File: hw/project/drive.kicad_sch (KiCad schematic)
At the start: 63 parts, among them Q10 STL110N10F7, Q5 STL110N10F7, Q6 STL110N10F7, Q7 STL110N10F7, Q8 STL110N10F7, Q9 STL110N10F7

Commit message: Continuing power revamp tomorrow
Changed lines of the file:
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@@
 		(exclude_from_sim no)
 		(at 220.98 38.1001 0)
-		(size 93.98 22.8453)
+		(size 93.98 20.3199)
 		(margins 0.9525 0.9525 0.9525 0.9525)
 		(stroke
@@
 		)
 	)
-	(text_box "Shunt Resistor\n\nFor a +/-50mV drop at +/-50A, R = 1.0m = 2.0m || 2.0m\n\nPair of parallel resistors, so 50A cts => 2.5W total (> 1.25W each)\n\nAt +/-2A, drop is +/-2mV, but use OPAMP configured in PGA mode (and voltage bias from internal DAC connection) to map to ADC range accordingly (bench testing will use way higher gain than while riding it fr)\n\nReason for not having an external resistor network for current sensing is it would mean a fixed gain, thus it could not be flexible for both bench testing and actually riding\n\nLayout Note: Using just regular 2-pin resistors despite the choice of symbol (4-pin kelvin sense)\n\nFW Note: Implement OCP (5.5.2 in UM2896) all in firmware by routing OPO_x to COMPx's non-inverting input and compared against the corresponding overcurrent threshoold voltage generated by an internal DAC. If an OCP event occurs, the comparator trips the TIM1_BKIN line, which shuts down the gate driver outputs"
+	(text_box "Shunt Resistor\n\nFor a +/-50mV drop at +/-50A, R = 1.0m = 2.0m || 2.0m\n\nPair of parallel resistors, so 50A cts => 2.5W total (> 1.25W each)\n\nAt +/-2A, drop is +/-2mV, but use OPAMP configured in PGA mode (and voltage bias from internal DAC connection) to map to ADC range accordingly (bench testing will use way higher gain than while riding it fr)\n\nReason for not having an external resistor network for current sensing is it would mean a fixed gain, thus it could not be flexible for both bench testing and actually riding\n\nLayout Note: Using just regular 2-pin resistors despite the choice of symbol (4-pin kelvin sense)\n\nFW Notes: \n- Implement OCP (5.5.2 in UM2896) all in firmware by routing OPO_x to COMPx's non-inverting input and compared against the corresponding overcurrent threshoold voltage generated by an internal DAC. If an OCP event occurs, the comparator trips the TIM1_BKIN line, which shuts down the gate driver outputs"
 		(exclude_from_sim no)
-		(at 220.98 60.9601 0)
-		(size 93.98 45.7199)
+		(at 220.98 58.4199 0)
+		(size 93.98 48.2601)
 		(margins 0.9525 0.9525 0.9525 0.9525)
 		(stroke

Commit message: Checkpoint: Ready to spec rest of power stage tom
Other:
- note added: "reconcile 22 vs 22.1k??"
- note added: "verify all with claude!!!!!!!!!!!!!!!!!!!!!!"
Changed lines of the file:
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@@
+		)
+	)
+	(text "verify all with claude!!!!!!!!!!!!!!!!!!!!!!"
+		(exclude_from_sim no)
+		(at -10.16 154.686 0)
+		(effects
+			(font
+				(size 1.27 1.27)
+				(color 255 4 4 1)
+			)
+			(justify left)
 		)
 	)
@@
 			)
 			(justify left top)
+		)
+	)
+	(text "reconcile 22 vs 22.1k??"
+		(exclude_from_sim no)
+		(at 13.97 171.196 0)
+		(effects
+			(font
+				(size 1.27 1.27)
+				(color 255 4 4 1)
+			)
+			(justify left)
 		)
 	)
@@
 		)
 	)
-	(text_box "Shunt Resistor\n\nFor a +/-50mV drop at +/-50A, R = 1.0m = 2.0m || 2.0m\n\nPair of parallel resistors, so 50A cts => 2.5W total (> 1.25W each)\n\nAt +/-2A, drop is +/-2mV, but use OPAMP configured in PGA mode (and voltage bias from internal DAC connection) to map to ADC range accordingly (bench testing will use way higher gain than while riding it fr)\n\nReason for not having an external resistor network for current sensing is it would mean a fixed gain, thus it could not be flexible for both bench testing and actually riding\n\nLayout Note: Using just regular 2-pin resistors despite the choice of symbol (4-pin kelvin sense)\n\nFW Notes: \n- Implement OCP (5.5.2 in UM2896) all in firmware by routing OPO_x to COMPx's non-inverting input and compared against the corresponding overcurrent threshoold voltage generated by an internal DAC. If an OCP event occurs, the comparator trips the TIM1_BKIN line, which shuts down the gate driver outputs"
+	(text_box "Shunt Resistor\n\nFor a +/-50mV drop at +/-50A, R = 1.0m = 2.0m || 2.0m\n\nPair of parallel resistors, so 50A cts => 2.5W total (> 1.25W each)\n\nAt +/-2A, drop is +/-2mV, but use OPAMP configured in PGA mode (and voltage bias from internal DAC connection) to map to ADC range accordingly (bench testing will use way higher gain than while riding it fr)\n\nReason for not having an external resistor network for current sensing is it would mean a fixed gain, thus it could not be flexible for both bench testing and actually riding\n\nLayout Note: \n- Using just regular 2-pin resistors despite the choice of symbol (4-pin kelvin sense)\n- Use Kelvin (differential trace pair) connections from inner pads to input pins\n\nFW Notes: \n- Implement OCP (5.5.2 in UM2896) all in firmware by routing OPO_x to COMPx's non-inverting input and compared against the corresponding overcurrent threshoold voltage generated by an internal DAC. If an OCP event occurs, the comparator trips the TIM1_BKIN line, which shuts down the gate driver outputs"
 		(exclude_from_sim no)
 		(at 220.98 58.4199 0)

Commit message: Spec bulk caps
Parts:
- added C20, C31: 22uF/100V, symbol Device:C_Small
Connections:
- net PGND: now also C20.2
- net VM: now also C20.1
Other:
- note added: "1210 or 2220"
- note added: "Bulk (Ceramic) Capacitor Bank"

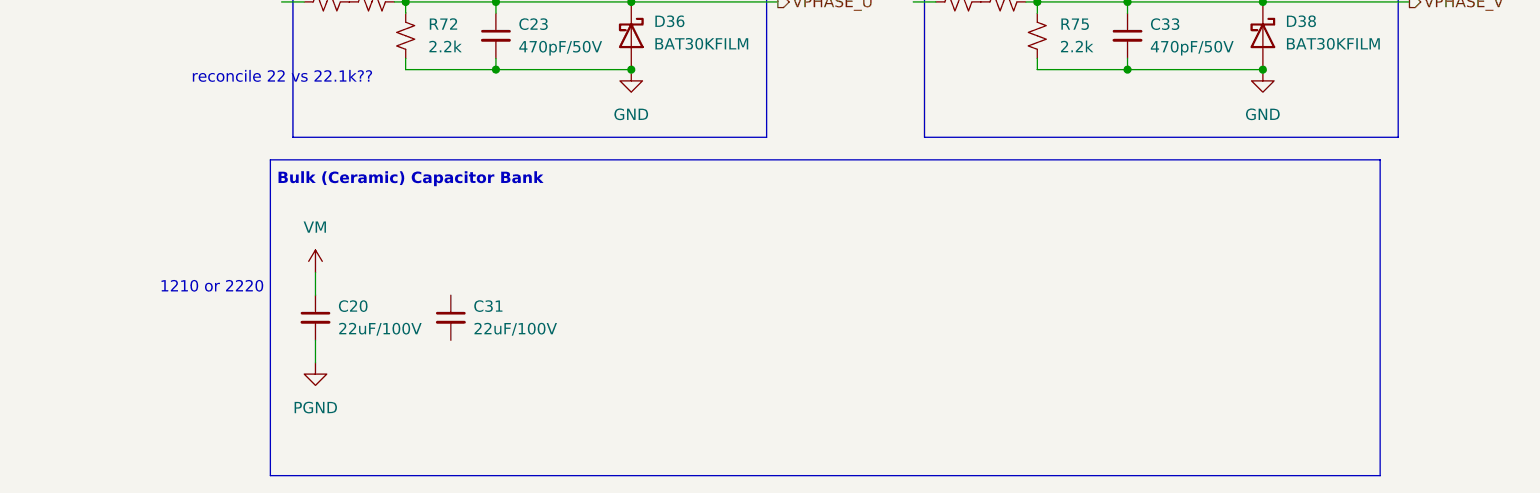
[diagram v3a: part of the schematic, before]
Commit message: Finalize 5V buck regulator
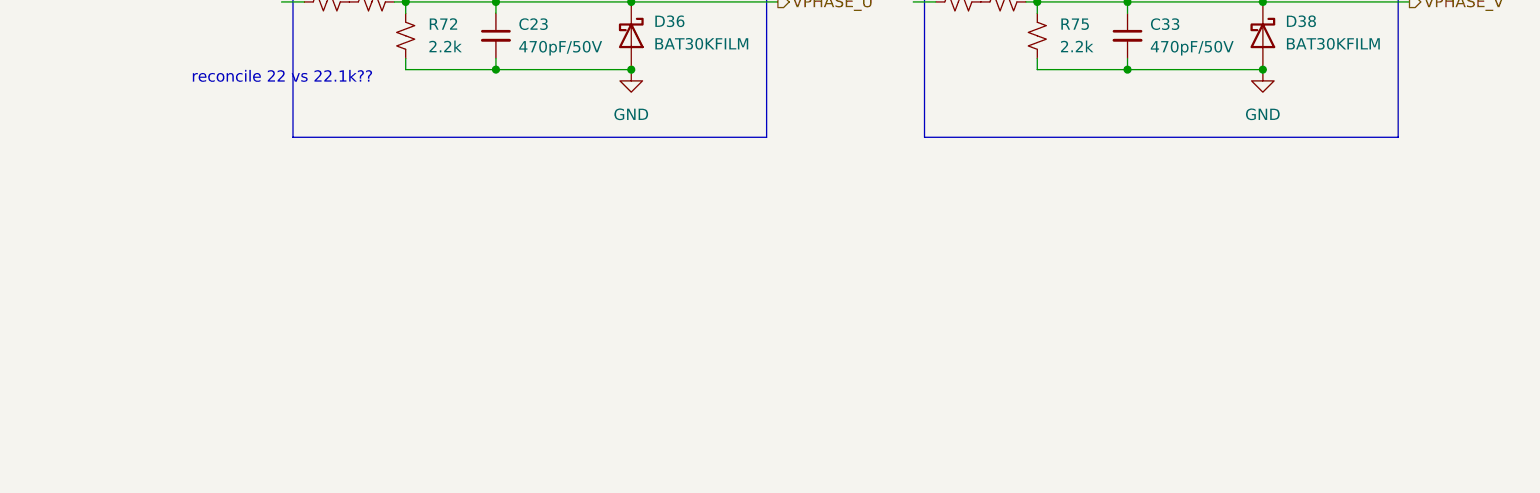
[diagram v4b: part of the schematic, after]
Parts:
- removed C20, C31: 22uF/100V, symbol Device:C_Small
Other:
- note removed: "1210 or 2220"
- note removed: "Bulk (Ceramic) Capacitor Bank"

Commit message: Spec LEDs
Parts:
- removed R52, R7, R70, R74, R76, R77: 22k, Resistor_SMD:R_0603_1608Metric, symbol Device:R_Small_US
- added R19, R24, R25, R26, R27, R30: 22.1k, Resistor_SMD:R_0603_1608Metric, symbol Device:R_Small_US
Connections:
- net U: now also R19.1
- net V: now also R25.1
- net VPHASE_U: now also R24.2
- net VPHASE_V: now also R26.2
- net VPHASE_W: now also R30.2
- net W: now also R27.1
- new net: R27.2, R30.1
- new net: R19.2, R24.1
- new net: R25.2, R26.1
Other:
- note added: "R2/(R1+R2) = 0.04741 {60} [V] -> {2.845} [V]"
- note removed: "R2/(R1+R2) = 1/21 = 0.04762 {60} [V] -> {2.857} [V]"
- note removed: "reconcile 22 vs 22.1k??"

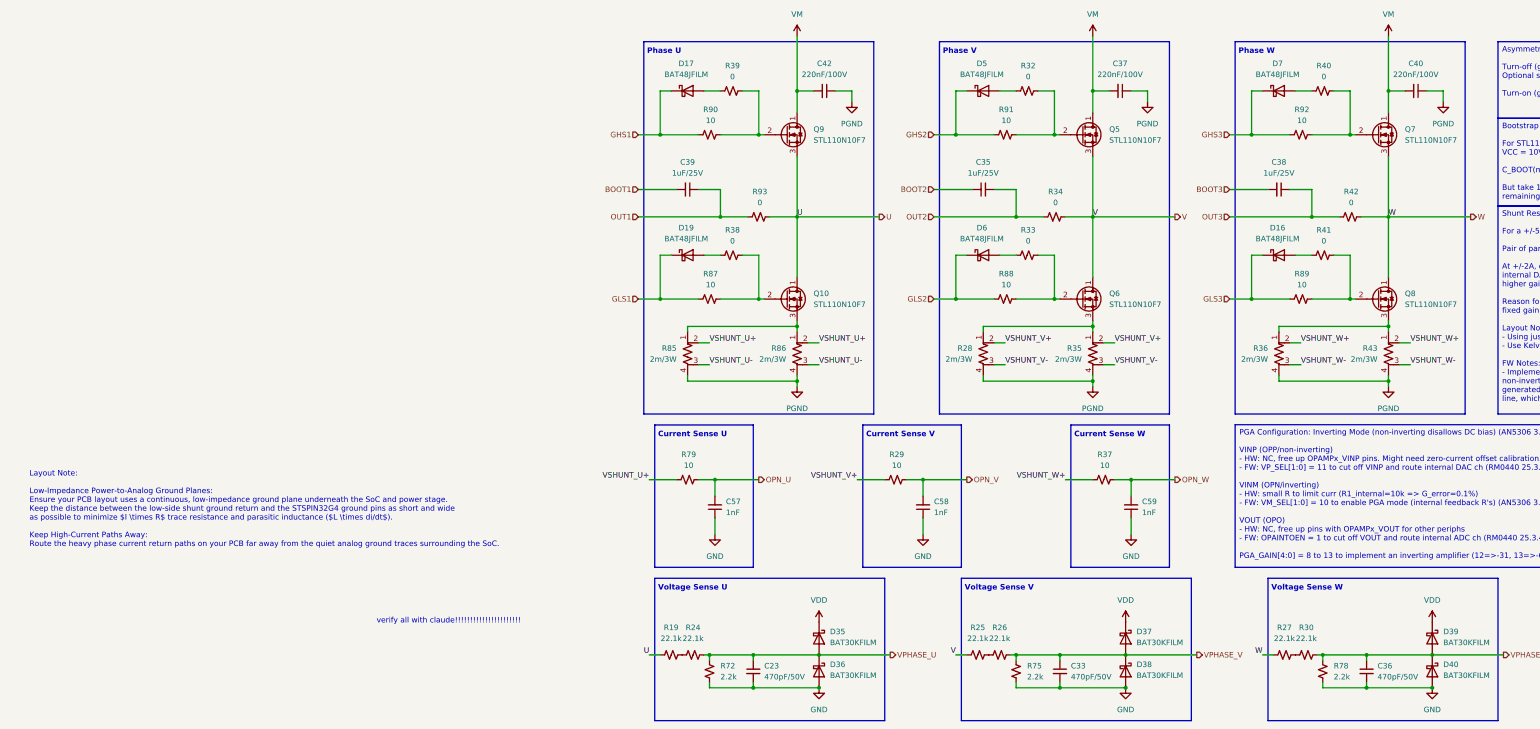
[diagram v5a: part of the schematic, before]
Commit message: Fixed annotations and H-labels
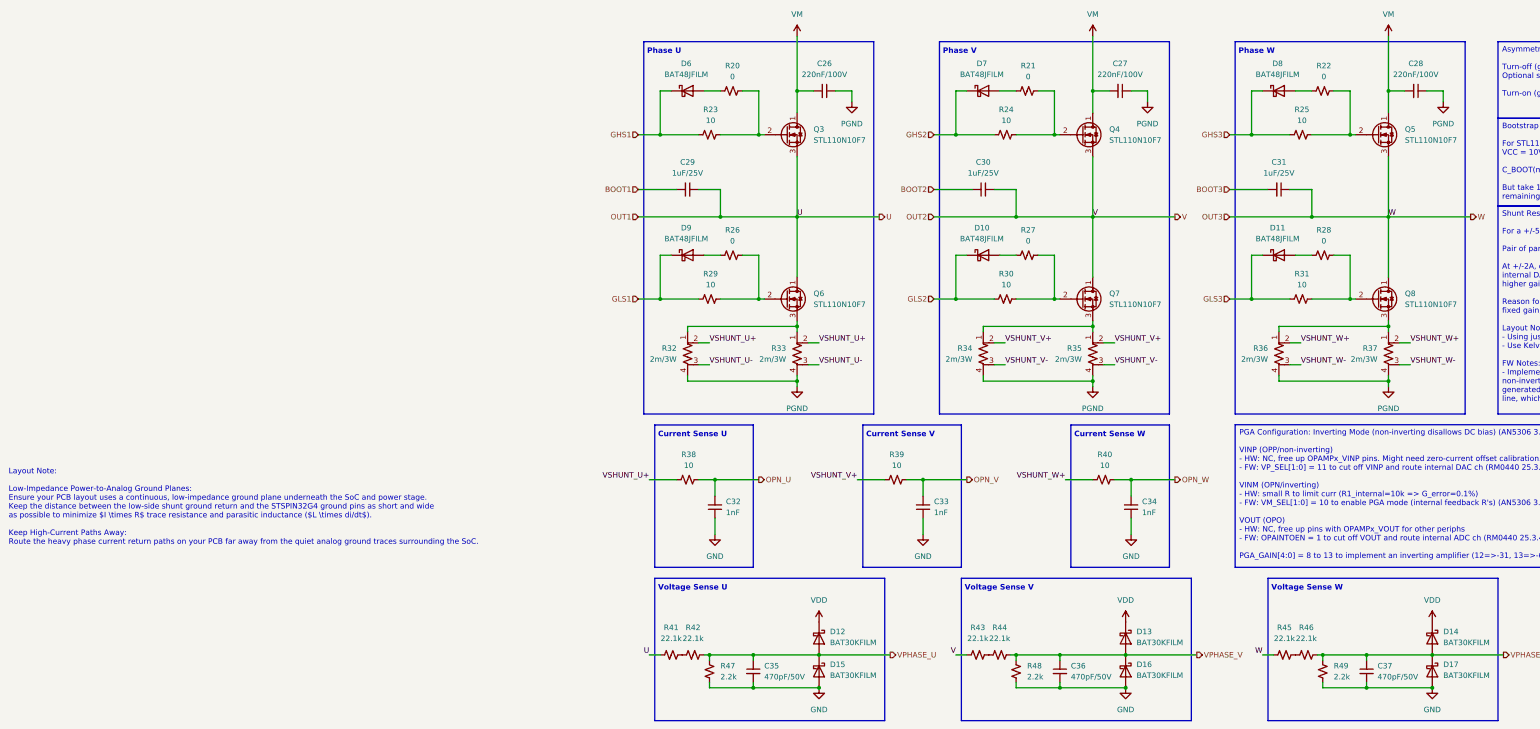
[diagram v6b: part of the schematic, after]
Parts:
- removed R34, R42, R93: 0, Resistor_SMD:R_0603_1608Metric, symbol Device:R_Small_US
- renumbered C42 to C26, C37 to C27, C40 to C28, C39 to C29, C35 to C30, C38 to C31, C57 to C32, C58 to C33, C59 to C34, C23 to C35, C33 to C36, C36 to C37, D6 to D10, D16 to D11, D35 to D12, D37 to D13, D39 to D14, D36 to D15, D38 to D16, D40 to D17, D17 to D6, D5 to D7, D7 to D8, D19 to D9, Q9 to Q3, Q5 to Q4, Q7 to Q5, Q10 to Q6, Q6 to Q7, R39 to R20, R32 to R21, R40 to R22, R90 to R23, R91 to R24, R92 to R25, R38 to R26, R33 to R27, R41 to R28, R87 to R29, R88 to R30, R89 to R31, R85 to R32, R86 to R33, R28 to R34, R43 to R37, R79 to R38, R29 to R39, R37 to R40, R19 to R41, R24 to R42, R25 to R43, R26 to R44, R27 to R45, R30 to R46, R72 to R47, R75 to R48, R78 to R49
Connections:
- net U is gone; now on net OUT1: Q3.3 (S), Q6.1 (D), R41.1
- net V is gone; now on net OUT2: Q4.3 (S), Q7.1 (D), R43.1
- net W is gone; now on net OUT3: Q5.3 (S), Q8.1 (D), R45.1
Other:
- note removed: "verify all with claude!!!!!!!!!!!!!!!!!!!!!!"

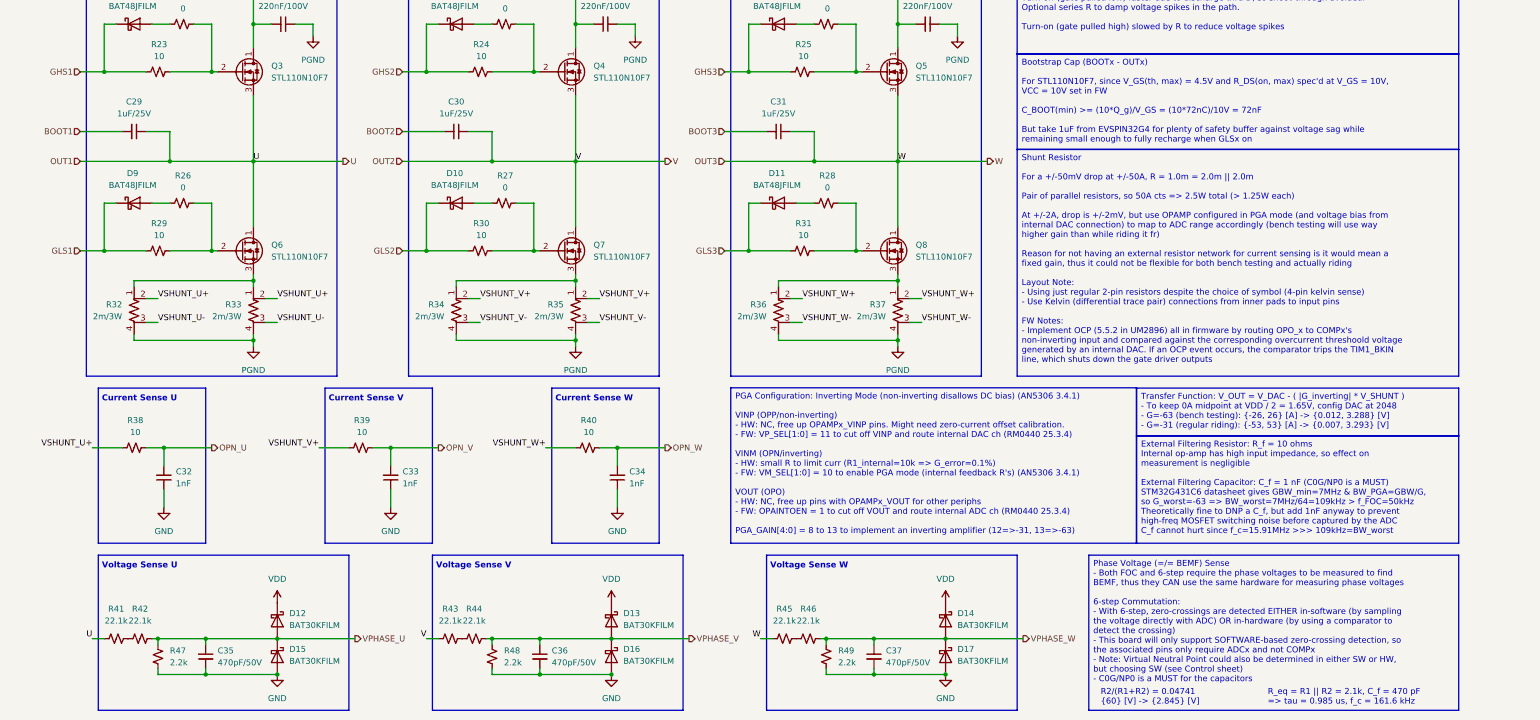
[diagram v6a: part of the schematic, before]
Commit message: Update shunt resistors and resolve ERC errors
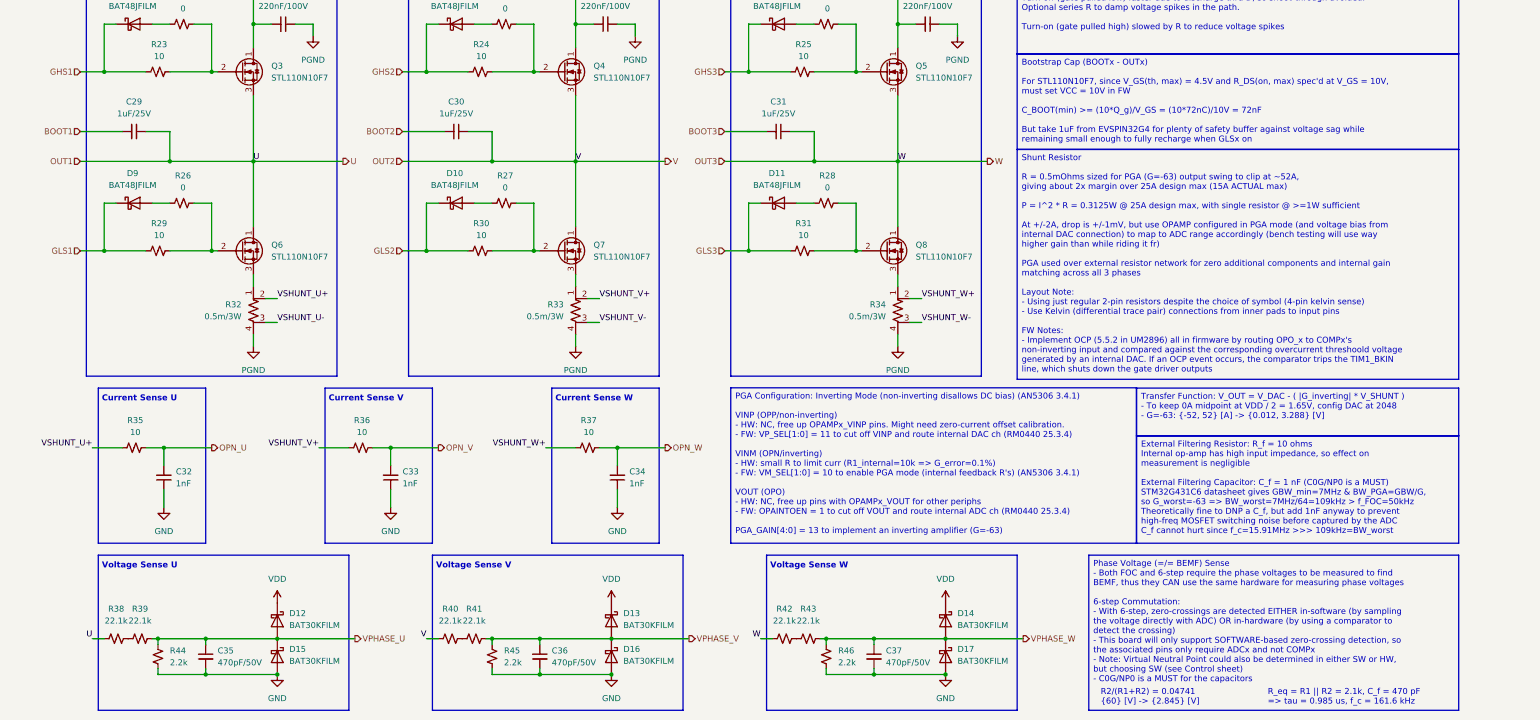
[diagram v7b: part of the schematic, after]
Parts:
- removed R32, R35, R36, R37: 2m/3W, Resistor_SMD:R_2512_6332Metric, symbol Device:R_Shunt_US
- added R33: 0.5m/3W, Resistor_SMD:R_2512_6332Metric, symbol Device:R_Shunt_US
- R32: renamed from R33; value 2m/3W -> 0.5m/3W
- R34: value 2m/3W -> 0.5m/3W
- renumbered R38 to R35, R39 to R36, R40 to R37, R41 to R38, R42 to R39, R43 to R40, R44 to R41, R45 to R42, R46 to R43, R47 to R44, R48 to R45, R49 to R46
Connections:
- net PGND: now also R33.4
- net VSHUNT_V+: now also R33.2; no longer R34.2
- net VSHUNT_V-: now also R33.3; no longer R34.3
- net VSHUNT_W+: now also R34.2
- net VSHUNT_W-: now also R34.3
- net at Q8.3 (S): now also R34.1
- net at Q7.3 (S): now also R33.1; no longer R34.1

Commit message: Clear PCB-add errors
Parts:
- R32, R33, R34: symbol Device:R_Shunt_US -> R_Shunt_US_two_pads:R_Shunt_US_two_pads
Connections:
- net PGND: now also R32.2, R33.2, R34.2; no longer R32.4, R33.4, R34.4
- net VSHUNT_U+: now also R32.1; no longer R32.2
- net VSHUNT_U-: now also R32.2; no longer R32.3
- net VSHUNT_V+: now also R33.1; no longer R33.2
- net VSHUNT_V-: now also R33.2; no longer R33.3
- net VSHUNT_W+: now also R34.1; no longer R34.2
- net VSHUNT_W-: now also R34.2; no longer R34.3
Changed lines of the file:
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@@
 	)
 	(symbol
-		(lib_id "Device:R_Shunt_US")
+		(lib_name "R_Shunt_US_two_pads_2")
+		(lib_id "R_Shunt_US_two_pads:R_Shunt_US_two_pads")
 		(at 195.58 92.71 0)
 		(unit 1)
@@
 			)
 		)
-		(property "Description" "0.0005 OHM 0.5% 3W 100PPM/C"
+		(property "Description" "Shunt resistor with Kelvin connections, US symbol"
 			(at 195.58 92.71 0)
 			(hide yes)
@@
 		(pin "1"
 		)
-		(pin "4"
+		(pin "2"
 		)
-		(pin "3"
+		(pin "1"
 		)
 		(pin "2"
@@
 	)
 	(symbol
-		(lib_id "Device:R_Shunt_US")
+		(lib_name "R_Shunt_US_two_pads_1")
+		(lib_id "R_Shunt_US_two_pads:R_Shunt_US_two_pads")
 		(at 127 92.71 0)
 		(unit 1)
@@
 			)
 		)
-		(property "Description" "0.0005 OHM 0.5% 3W 100PPM/C"
+		(property "Description" "Shunt resistor with Kelvin connections, US symbol"
 			(at 127 92.71 0)
 			(hide yes)
@@
 		(pin "1"
 		)
-		(pin "4"
+		(pin "1"
 		)
-		(pin "3"
+		(pin "2"
 		)
 		(pin "2"
@@
 	)
 	(symbol
-		(lib_id "Device:R_Shunt_US")
+		(lib_id "R_Shunt_US_two_pads:R_Shunt_US_two_pads")
 		(at 58.42 92.71 0)
 		(unit 1)
@@
 			)
 		)
-		(property "Description" "0.0005 OHM 0.5% 3W 100PPM/C"
+		(property "Description" "Shunt resistor with Kelvin connections, US symbol"
 			(at 58.42 92.71 0)
 			(hide yes)
@@
 		(pin "1"
 		)
-		(pin "4"
+		(pin "1"
 		)
-		(pin "3"
+		(pin "2"
 		)
 		(pin "2"
